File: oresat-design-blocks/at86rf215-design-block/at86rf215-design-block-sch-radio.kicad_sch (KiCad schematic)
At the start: 45 parts, among them J1 SMA, J10 Conn_01x08, J11 Conn_01x05, J12 Conn_01x08, J2 USB4105-GF-A, J3 Conn_01x06, J6 Conn_01x06, J9 Screw_Terminal_01x02, SW1 RESET, U1 AT86RF215, U2 LP2985AIM5-1.8_NOPB, X1 TXETALSANF-26.000000

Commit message: Last minute fixes and polishing.
Added capacitor and LED BOM part numbers. Fixed balun footprint and layout; had the wrong idea of how to lay it out. Now more closely matches the evaluation board. Also everything now 50 ohms, even the diff pairs. Fixed solder mask over RF. Better silkscreen too.
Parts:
- C1, C10, C11, C12, C13, C5, C6, C7, C8, C9: DPN 587-3472-1-ND -> 399-6853-1-ND; MFR Taiyo Yuden -> KEMET; MPN TMK107BJ104KAHT -> C0603C104J5RACAUTO
- C14: DPN 1276-1784-1-ND -> 399-C0603C475K8PAC7411CT-ND; MFR Samsung Electro-Mechanics -> KEMET; MPN CL10A475KO8NNNC -> C0603C475K8PAC7411
- C15: DPN 399-14102-1-ND -> 399-12983-1-ND; MPN C0603C103J3GECAUTO -> C0603C103J5RACAUTO
- C16: DPN 587-3473-1-ND -> 399-C0603C105K3RACTUCT-ND; MFR Taiyo Yuden -> KEMET; MPN TMK107BJ105KAHT -> C0603C105K3RACTU
- C2: DIS (none) -> DigiKey; DPN (none) -> 399-17595-1-ND; MFR (none) -> KEMET; MPN (none) -> C0603C472J5RACAUTO
- C3: DIS (none) -> DigiKey; DPN (none) -> 399-12989-1-ND; MFR (none) -> KEMET; MPN (none) -> C0603C102J5RACAUTO
- C4: DIS (none) -> DigiKey; DPN (none) -> 399-C0603C229B5HACAUTOCT-ND; MFR (none) -> KEMET; MPN (none) -> C0603C229B5HACAUTO
- D1: DIS (none) -> DigiKey; DPN (none) -> 732-4971-1-ND; MFR (none) -> Wurth; MPN (none) -> 150060GS75000

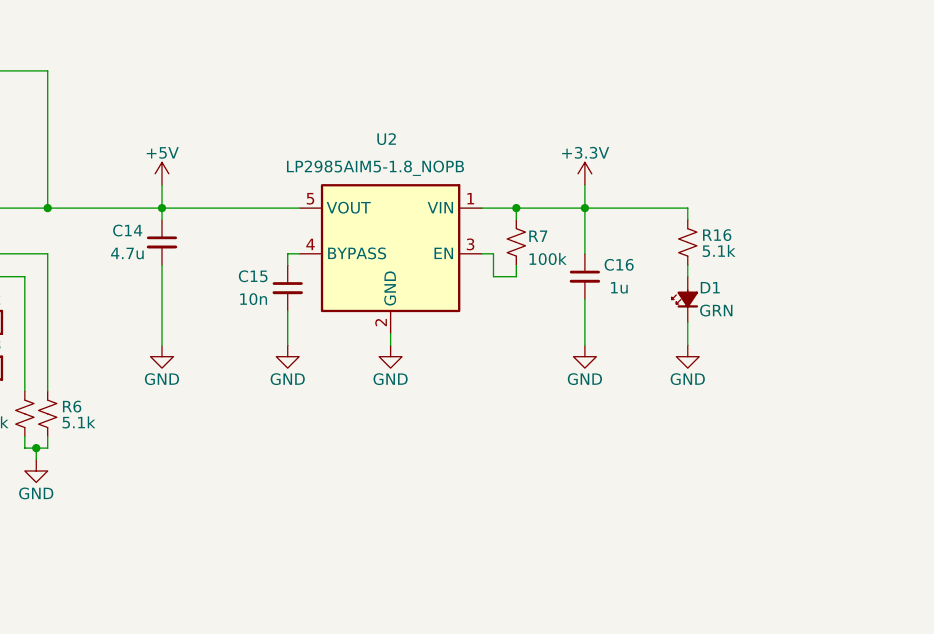
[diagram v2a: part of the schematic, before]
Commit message: fixed USBC power LDO vin vout swap
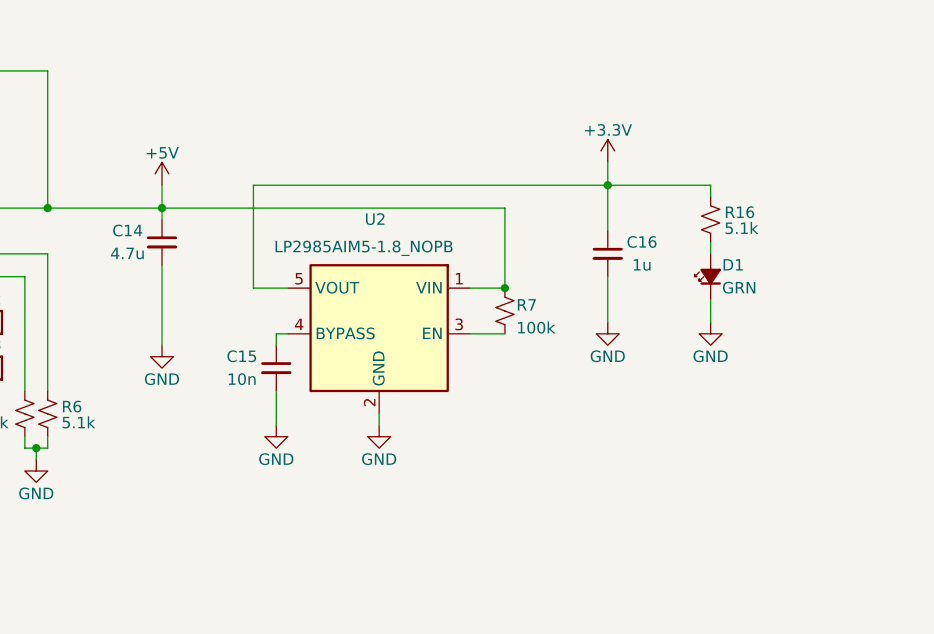
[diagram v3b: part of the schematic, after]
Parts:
- TP1, TP10, TP2, TP3: value ~ -> (none)
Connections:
- net +3.3V: now also U2.5 (VOUT); no longer R7.1, U2.1 (VIN)
- net +5V: now also R7.1, U2.1 (VIN); no longer U2.5 (VOUT)
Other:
- moved on the sheet: C15, C16, D1, R16, R7, U2
